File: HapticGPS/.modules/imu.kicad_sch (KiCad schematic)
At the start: 7 parts, among them U6 LSM6

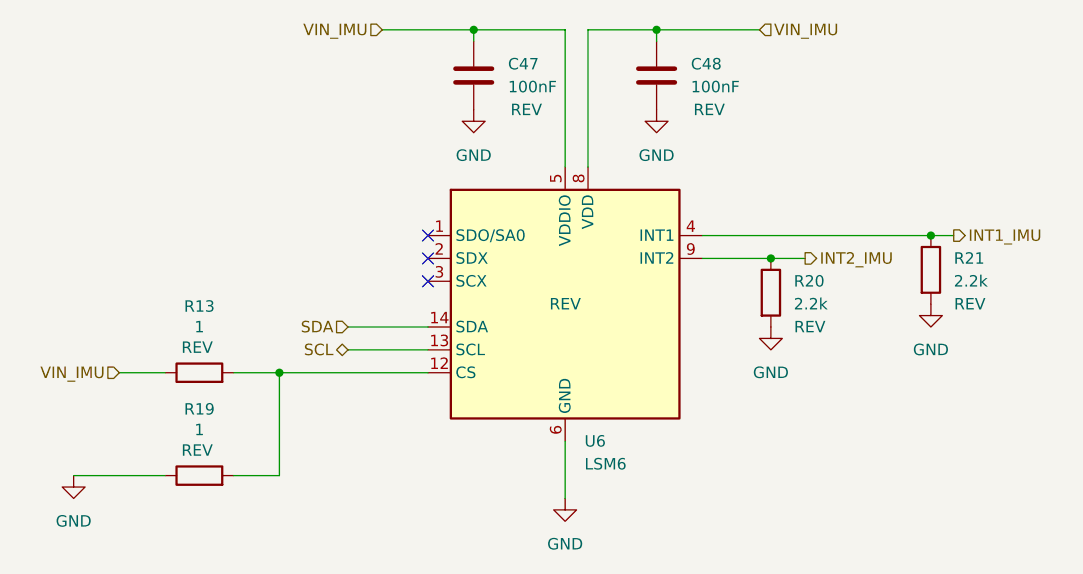
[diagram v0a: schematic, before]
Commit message: eliminating GPS, and second piezo driver
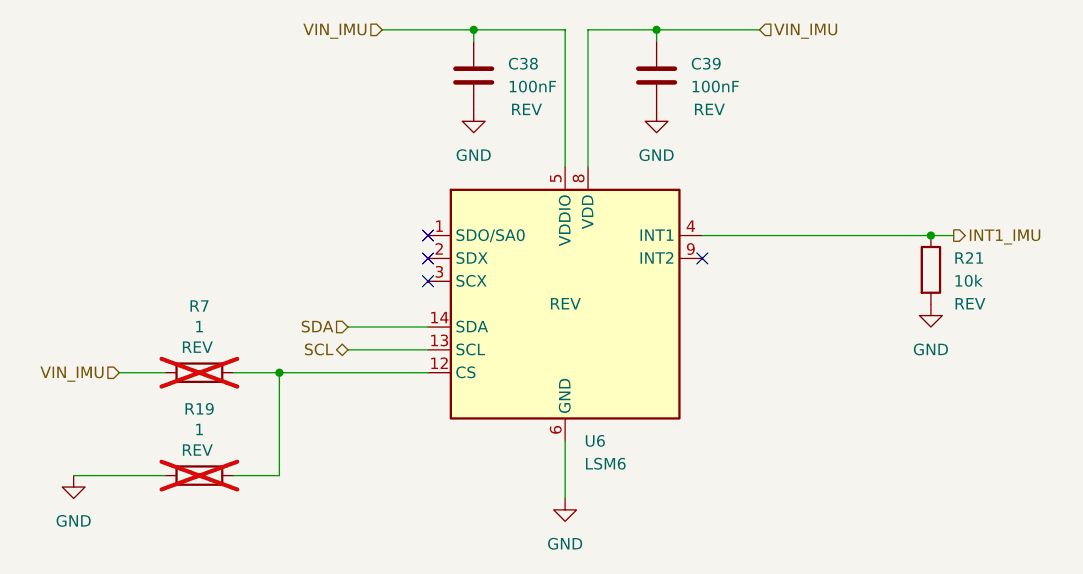
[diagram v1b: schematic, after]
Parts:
- removed C47, C48: 100nF, Capacitor_SMD:C_0603_1608Metric, symbol Device:C
- removed R13: 1, Resistor_SMD:R_0805_2012Metric, symbol Device:R
- removed R20: 2.2k, Capacitor_SMD:C_0603_1608Metric, symbol Device:R
- added C38, C39: 100nF, Capacitor_SMD:C_0402_1005Metric, symbol Device:C
- added R7: 1, Resistor_SMD:R_0402_1005Metric, symbol Device:R
- R19: footprint Resistor_SMD:R_0805_2012Metric -> Resistor_SMD:R_0402_1005Metric; now not fitted; now left out of the parts list
- R21: value 2.2k -> 10k; footprint Capacitor_SMD:C_0603_1608Metric -> Resistor_SMD:R_0402_1005Metric; Number Part CRGCQ0603F2K2 -> RC0402FR-0710KL
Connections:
- net GND: now also C38.2, C39.2
- net VIN_IMU: now also C38.1, C39.1, R7.1
- net at R19.2, U6.12 (CS): now also R7.2
- net INT2_IMU: no longer names the net of U6.9 (INT2)
- no-connect marks 3 -> 4
